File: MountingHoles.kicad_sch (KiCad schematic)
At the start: 8 parts

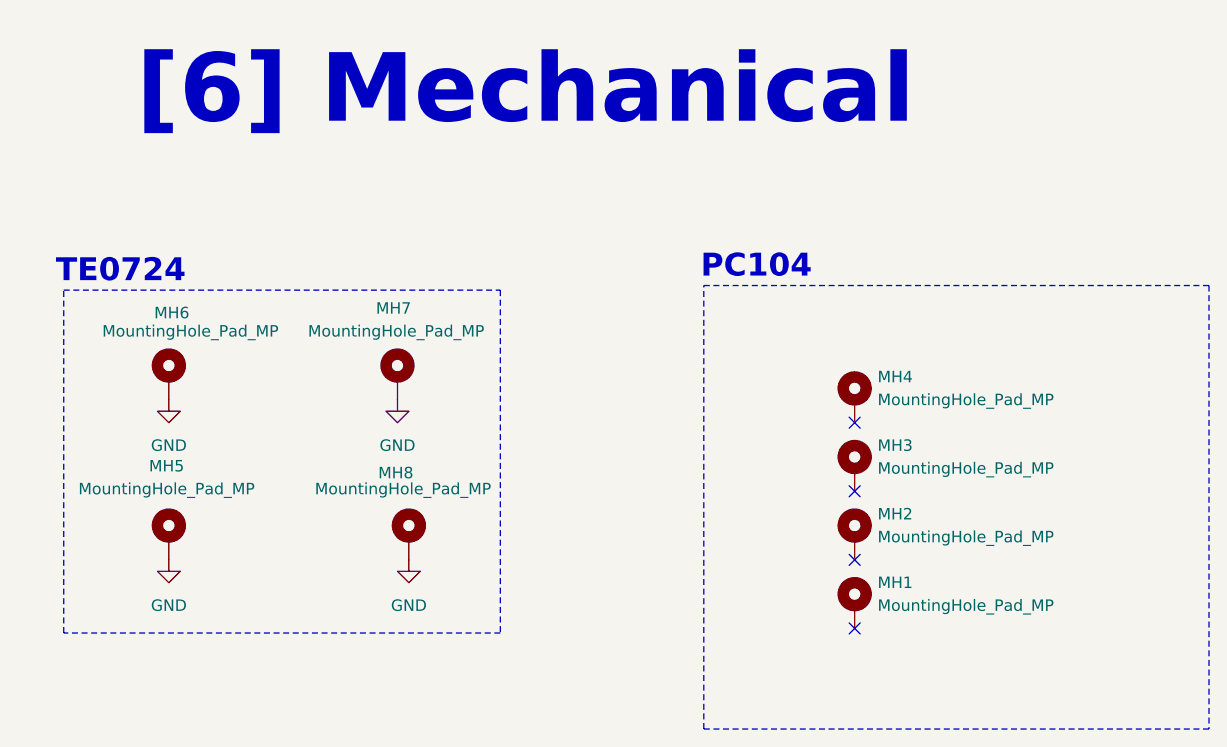
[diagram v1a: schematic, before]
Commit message: Added Level Shifter for SD card
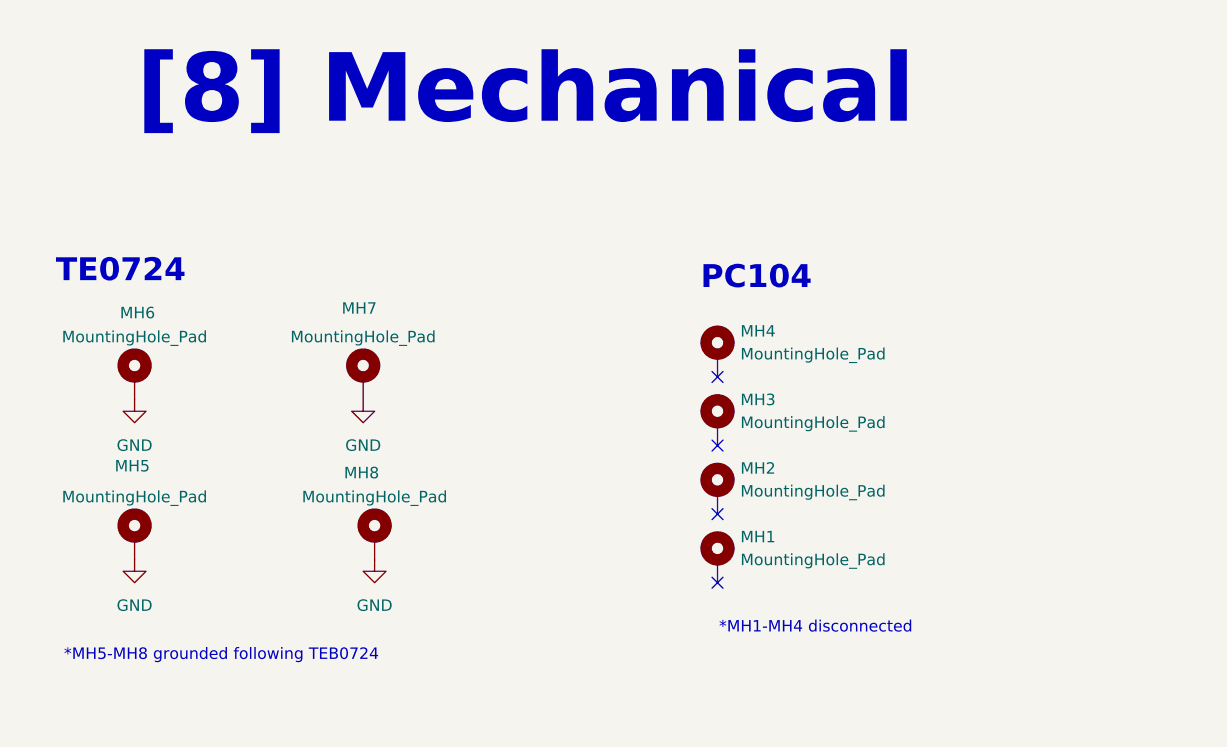
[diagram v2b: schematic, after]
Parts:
- MH1, MH2, MH3, MH4, MH5, MH6, MH7, MH8: value MountingHole_Pad_MP -> MountingHole_Pad; symbol Mechanical:MountingHole_Pad_MP -> Mechanical:MountingHole_Pad
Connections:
- net GND: now also MH5.1, MH6.1, MH7.1, MH8.1; no longer MH5.MP, MH6.MP, MH7.MP, MH8.MP
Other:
- note added: "*MH1-MH4 disconnected"
- note added: "*MH5-MH8 grounded following TEB0724"
- note added: "[8] Mechanical"
- note removed: "[6] Mechanical"
- moved on the sheet: MH1, MH2, MH3, MH4, MH5, MH6, MH7, MH8
